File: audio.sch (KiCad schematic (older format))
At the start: 25 parts, among them U1 UDA1334A

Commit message: Update symbols to remove layout warnings.
Change shoulder button switches to SPST (two pin) switches to match the
side actuated devices. Change the speaker symbol pin names to '+' and
'-' to match the footprint.
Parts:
- LS1, LS2: symbol Device:Speaker -> rpi-shell:speaker
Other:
- moved on the sheet: LS1, LS2
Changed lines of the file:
@@
 $EndComp
 $Comp
-L Device:Speaker LS1
+L rpi-shell:speaker LS1
 U 1 1 606892D7
-P 8450 2350
-F 0 "LS1" H 8620 2346 50  0000 L CNN
-F 1 "Speaker" H 8620 2255 50  0000 L CNN
-F 2 "SMS-1308MS-2-R:SMS-1308MS-2-R" H 8450 2150 50  0001 C CNN
-F 3 "~" H 8440 2300 50  0001 C CNN
-	1    8450 2350
+P 8450 2400
+F 0 "LS1" H 8620 2396 50  0000 L CNN
+F 1 "Speaker" H 8620 2305 50  0000 L CNN
+F 2 "SMS-1308MS-2-R:SMS-1308MS-2-R" H 8450 2200 50  0001 C CNN
+F 3 "~" H 8440 2350 50  0001 C CNN
+	1    8450 2400
 	1    0    0    -1
 $EndComp
@@
 $EndComp
 $Comp
-L Device:Speaker LS2
+L rpi-shell:speaker LS2
 U 1 1 606DD665
-P 8450 5500
-F 0 "LS2" H 8620 5496 50  0000 L CNN
-F 1 "Speaker" H 8620 5405 50  0000 L CNN
-F 2 "SMS-1308MS-2-R:SMS-1308MS-2-R" H 8450 5300 50  0001 C CNN
-F 3 "~" H 8440 5450 50  0001 C CNN
-	1    8450 5500
-	1    0    0    -1
-$EndComp
+P 8450 5550
+F 0 "LS2" H 8620 5546 50  0000 L CNN
+F 1 "Speaker" H 8620 5455 50  0000 L CNN
+F 2 "SMS-1308MS-2-R:SMS-1308MS-2-R" H 8450 5350 50  0001 C CNN
+F 3 "~" H 8440 5500 50  0001 C CNN
+	1    8450 5550
+	1    0    0    -1
+$EndComp

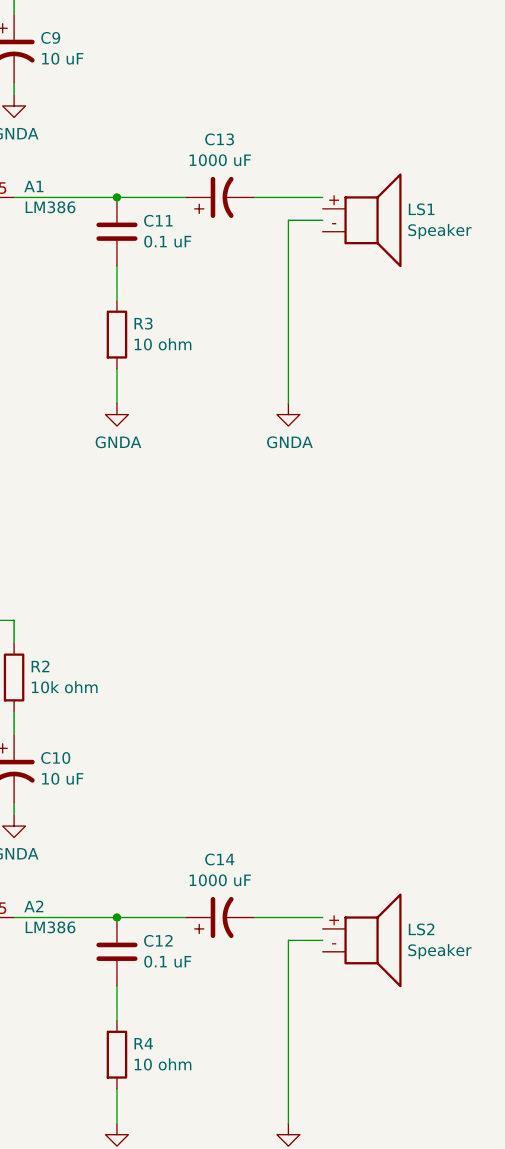
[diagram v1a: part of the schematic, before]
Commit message: Add adafruit footprint.
Add Adafruit footprint made from Adafruit PCB model. Fix UDA1334A pin
numbering to match the footprint. This also exposes an issue where the
wsel, bclk, and din pins are not connected to anything because it is
marked as NC on the top level. This should maybe be replaced with male
pin header so dupont connectors can be used to attach these pins to the
raspberry pi.
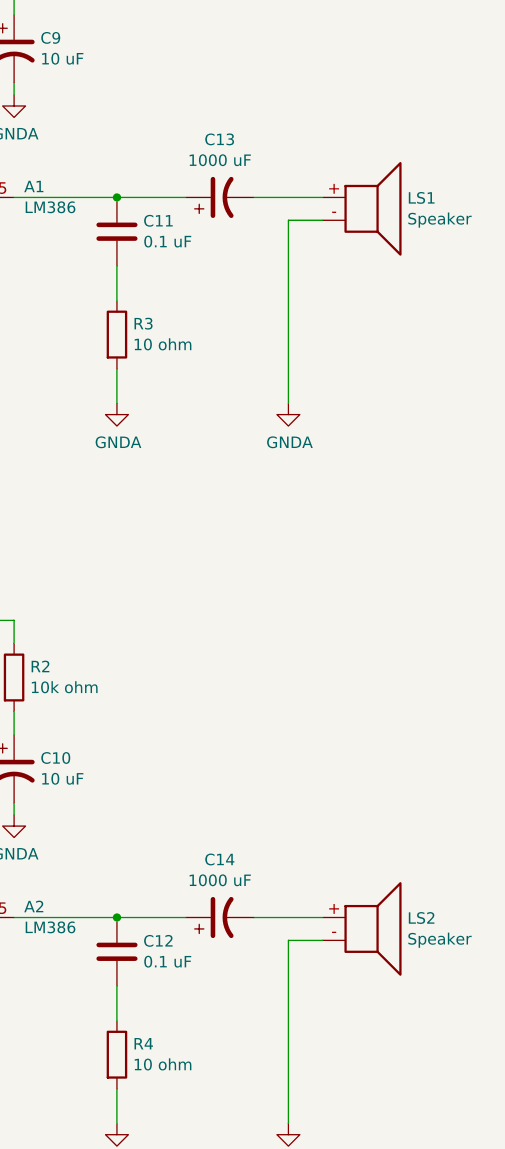
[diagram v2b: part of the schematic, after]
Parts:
- U1: footprint (none) -> rpi-shell-v1-sockets:UDA1334A
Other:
- moved on the sheet: LS1, LS2
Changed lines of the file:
@@
 L rpi-shell:speaker LS1
 U 1 1 606892D7
-P 8450 2400
-F 0 "LS1" H 8620 2396 50  0000 L CNN
-F 1 "Speaker" H 8620 2305 50  0000 L CNN
-F 2 "SMS-1308MS-2-R:SMS-1308MS-2-R" H 8450 2200 50  0001 C CNN
-F 3 "~" H 8440 2350 50  0001 C CNN
-	1    8450 2400
+P 8450 2350
+F 0 "LS1" H 8620 2346 50  0000 L CNN
+F 1 "Speaker" H 8620 2255 50  0000 L CNN
+F 2 "SMS-1308MS-2-R:SMS-1308MS-2-R" H 8450 2150 50  0001 C CNN
+F 3 "~" H 8440 2300 50  0001 C CNN
+	1    8450 2350
 	1    0    0    -1
 $EndComp
@@
 L rpi-shell:speaker LS2
 U 1 1 606DD665
-P 8450 5550
-F 0 "LS2" H 8620 5546 50  0000 L CNN
-F 1 "Speaker" H 8620 5455 50  0000 L CNN
-F 2 "SMS-1308MS-2-R:SMS-1308MS-2-R" H 8450 5350 50  0001 C CNN
-F 3 "~" H 8440 5500 50  0001 C CNN
-	1    8450 5550
+P 8450 5500
+F 0 "LS2" H 8620 5496 50  0000 L CNN
+F 1 "Speaker" H 8620 5405 50  0000 L CNN
+F 2 "SMS-1308MS-2-R:SMS-1308MS-2-R" H 8450 5300 50  0001 C CNN
+F 3 "~" H 8440 5450 50  0001 C CNN
+	1    8450 5500
 	1    0    0    -1
 $EndComp
@@
 F 0 "U1" H 2350 4665 50  0000 C CNN
 F 1 "UDA1334A" H 2350 4574 50  0000 C CNN
-F 2 "" H 2150 4550 50  0001 C CNN
+F 2 "rpi-shell-v1-sockets:UDA1334A" H 2150 4550 50  0001 C CNN
 F 3 "" H 2150 4550 50  0001 C CNN
 	1    2350 3850

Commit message: Add 3ds button cross footprint.
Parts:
- U1: symbol adafruit:UDA1334A -> rpi-shell-v1-rescue:UDA1334A-adafruit
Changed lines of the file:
@@
 	4800 5400 6300 5400
 $Comp
-L adafruit:UDA1334A U1
+L rpi-shell-v1-rescue:UDA1334A-adafruit U1
 U 1 1 6067F8B5
 P 2350 3850
+AR Path="/6067F8B5" Ref="U1"  Part="1"
+AR Path="/6068502A/6067F8B5" Ref="U1"  Part="1"
 F 0 "U1" H 2350 4665 50  0000 C CNN
 F 1 "UDA1334A" H 2350 4574 50  0000 C CNN
